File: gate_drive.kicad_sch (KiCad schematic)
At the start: 56 parts, among them J2 DSUB-37_Socket, U5 UCC27524DR, U6 UCC27524DR, U7 UCC27524DR, U8 SN74LVC1G11DBVR

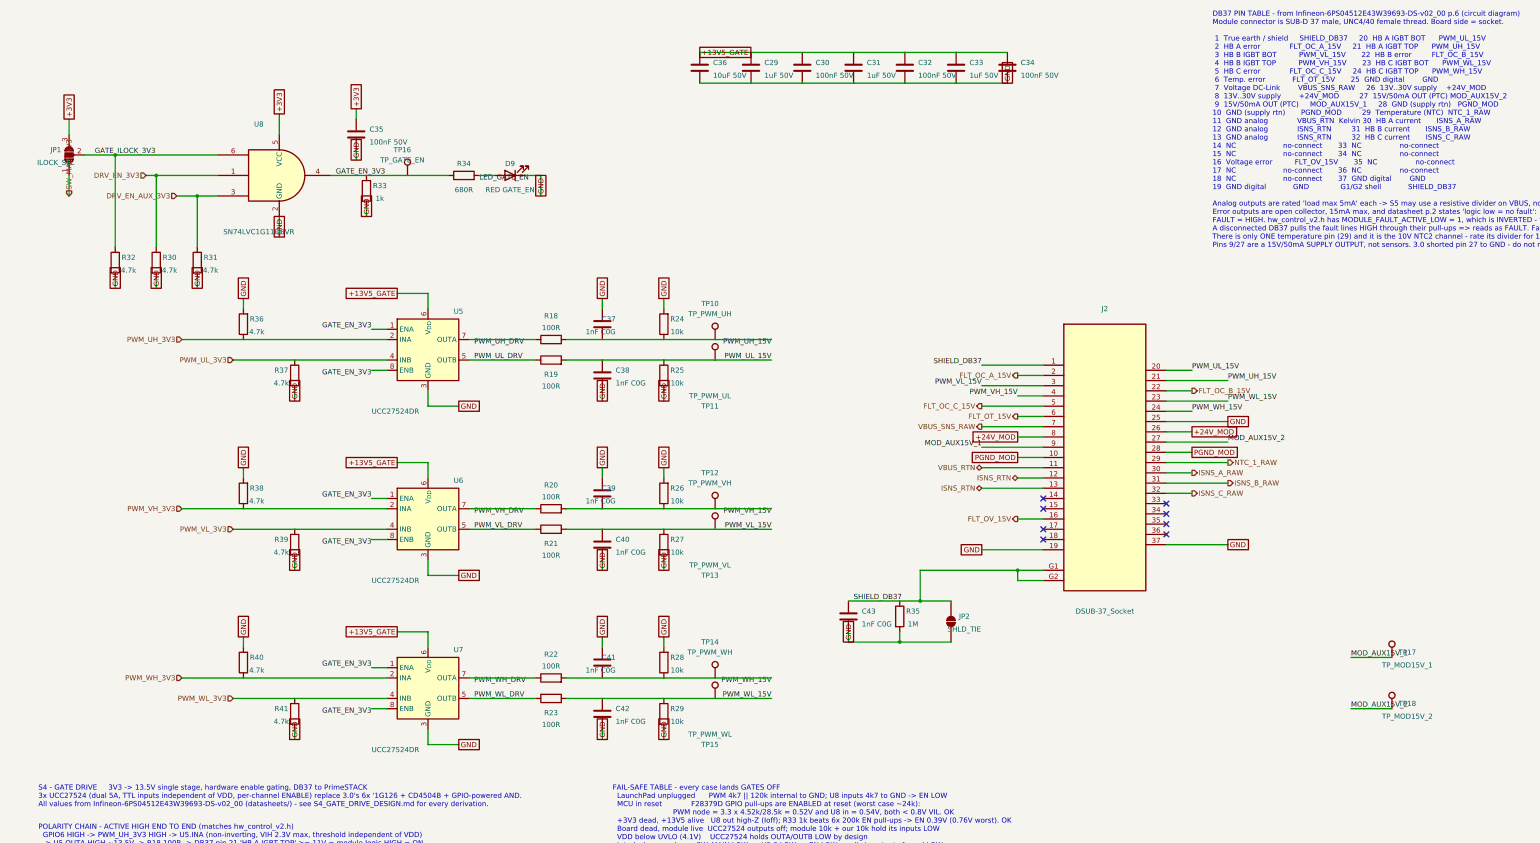
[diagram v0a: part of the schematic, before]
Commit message: S8: vehicle_io sheet, schematic freeze - CAN, isolated cockpit inputs, ECU 5 V feed
vehicle_io: J5 DEUTSCH DTM13-08PA-R004 (8-way, key A - way-count keyed against
the two 12-way keys already used), SN65HVD230 CAN-A front-end with ACT45B
common-mode choke, PSM712 TVS and a bridged-jumper 120 R termination, two
identical optically isolated inputs (LTV-817S high-side, 2.2k pull-down,
SN74LVC2G17 Schmitt - every failure reads LOW), and the provisional +5V_VEH
feed (SS34 back-feed block + 0.2 A polyfuse + SMAJ5.0A). 30 parts, 6 new
symbols, 5 new footprints (DTM13-08PA derived from TE's drawing: it is a
vertical-flange right-angle part with 6.35 mm row spacing, not the flat-base
4.19 mm grid S7's table assumed - corrected there).

Netlist 201/835 -> 220/914, every new net verified node by node; project ERC
--severity-all = 0. golden.net re-baselined. Pin map cross-checked on the
netlist side: 29/29 signals on the SPRUI77 pin the firmware expects. BOM/JLC
audit: 293 placements on 63 LCSC lines (29 Basic / 4 Preferred / 30 Extended),
5 consigned, 0 empty; the 2.2 nF C0G line (C107043, 4 in stock) moved to
Murata C77033 on all ten anti-alias caps.

Tooling: KiCad's vertical-label justify rule was measured and fixed in
layoutlib (every downward GND flag had been drawn over its part on every S7.5
sheet), field justify now follows mirror/180, missing-justify insertion fixed,
and note texts are addressed by content instead of file index. All six older
sheets regenerated: notes identical to HEAD, netlist identical, ERC 0.

Co-Authored-By: Claude Fable 5.1 <noreply@anthropic.com>
Claude-Session: https://claude.ai/code/session_01BbqAgraN6LAYLruGRERKDp
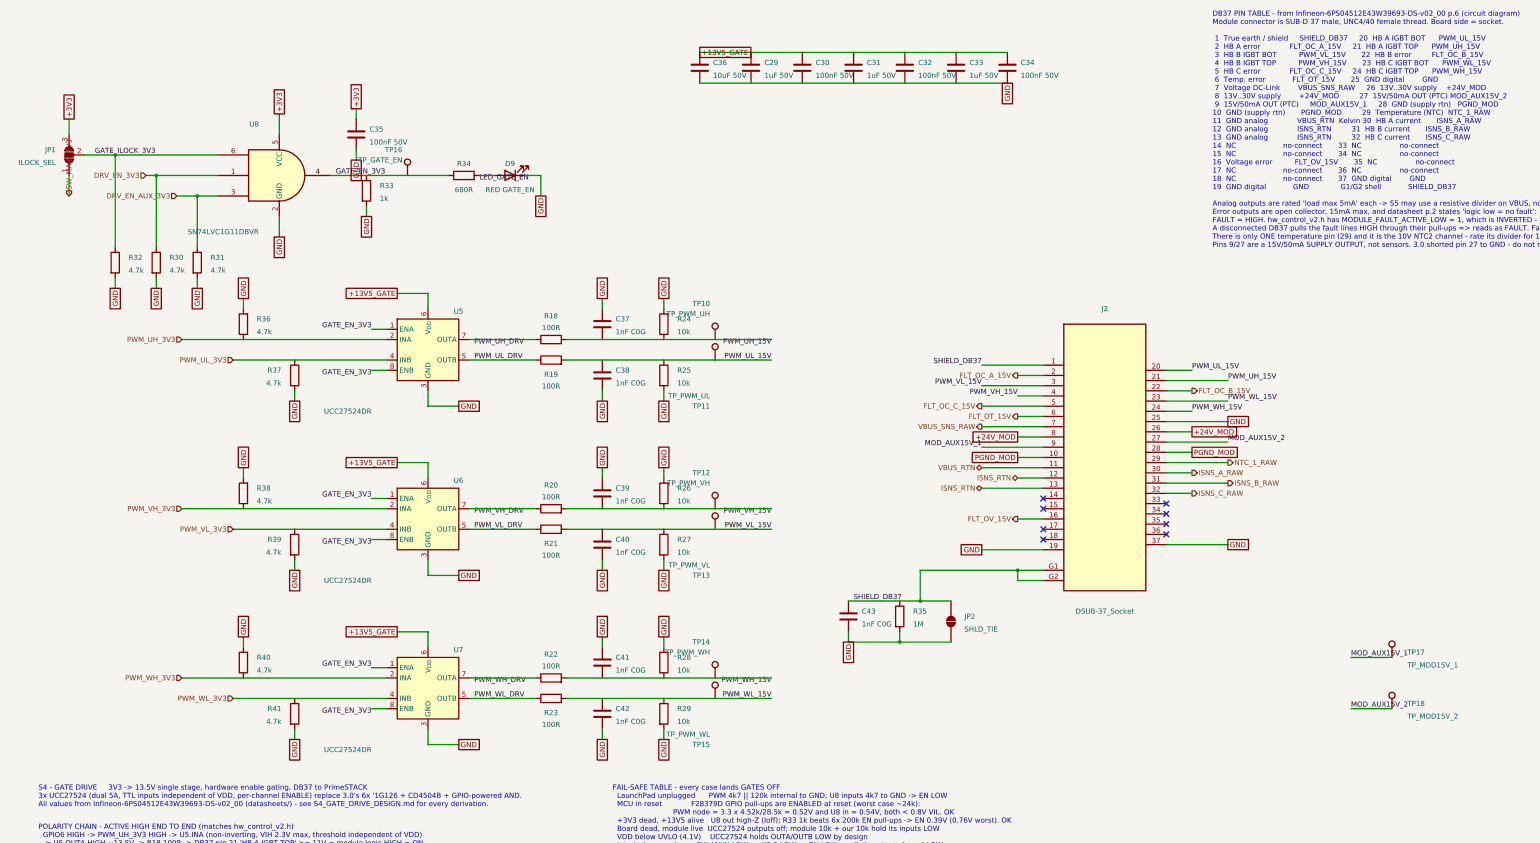
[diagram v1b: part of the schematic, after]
